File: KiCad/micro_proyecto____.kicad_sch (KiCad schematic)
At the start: 37 parts, among them J1 Conn_01x02, J2 Conn_01x05, J3 Conn_01x02, J4 Conn_01x02, J5 Conn_01x02, J6 Conn_01x02, SW1 SW_Push, SW2 SW_Push, SW3 SW_Push, SW4 SW_Push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

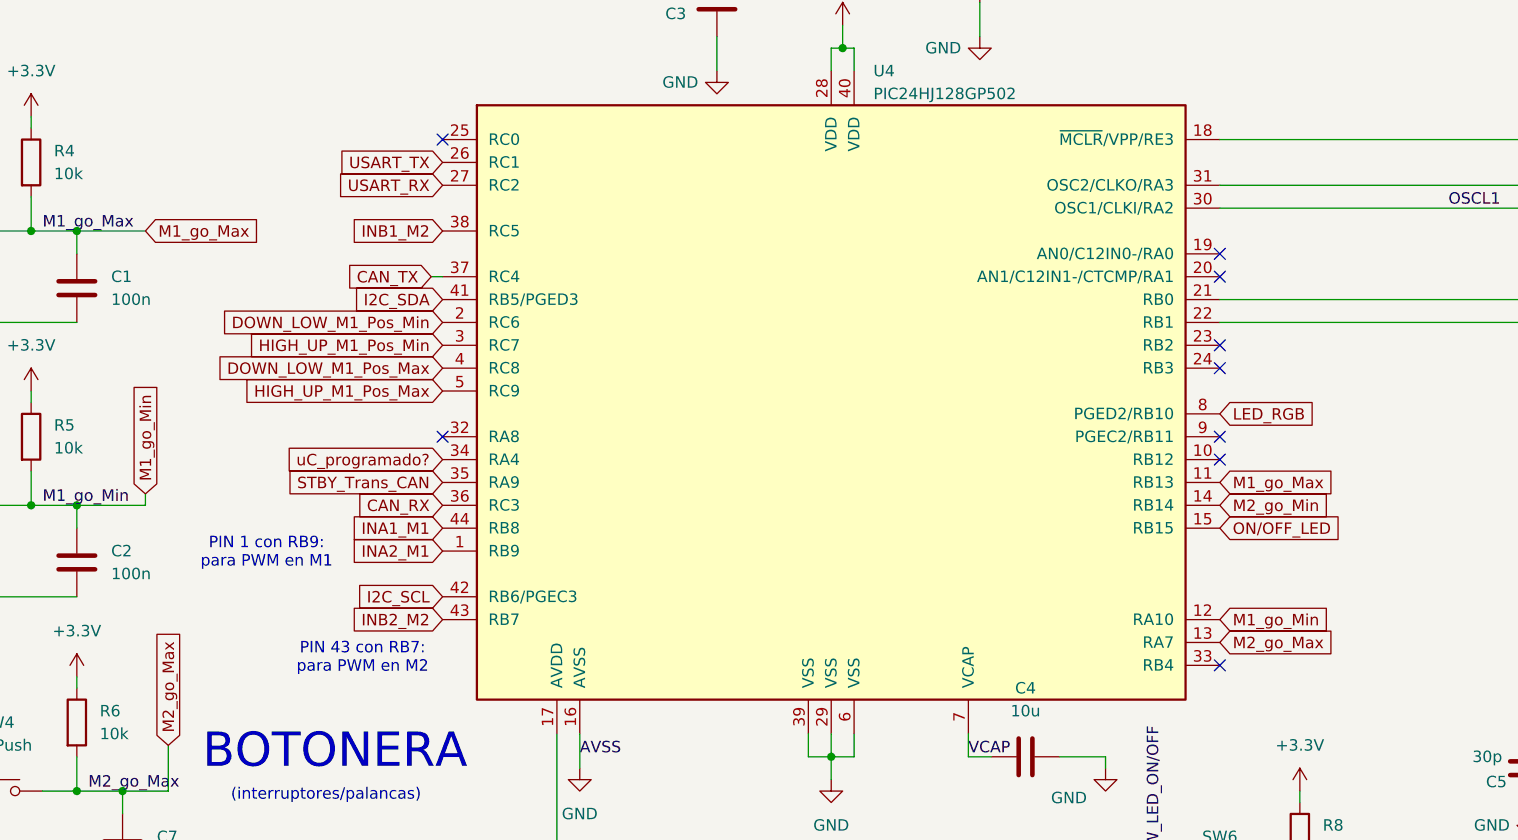
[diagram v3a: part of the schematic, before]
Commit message: PCB casi acabada, despues de revisión de ayer 27/04 y cambio en componente CAN, que se vera reflejado en README y en DB
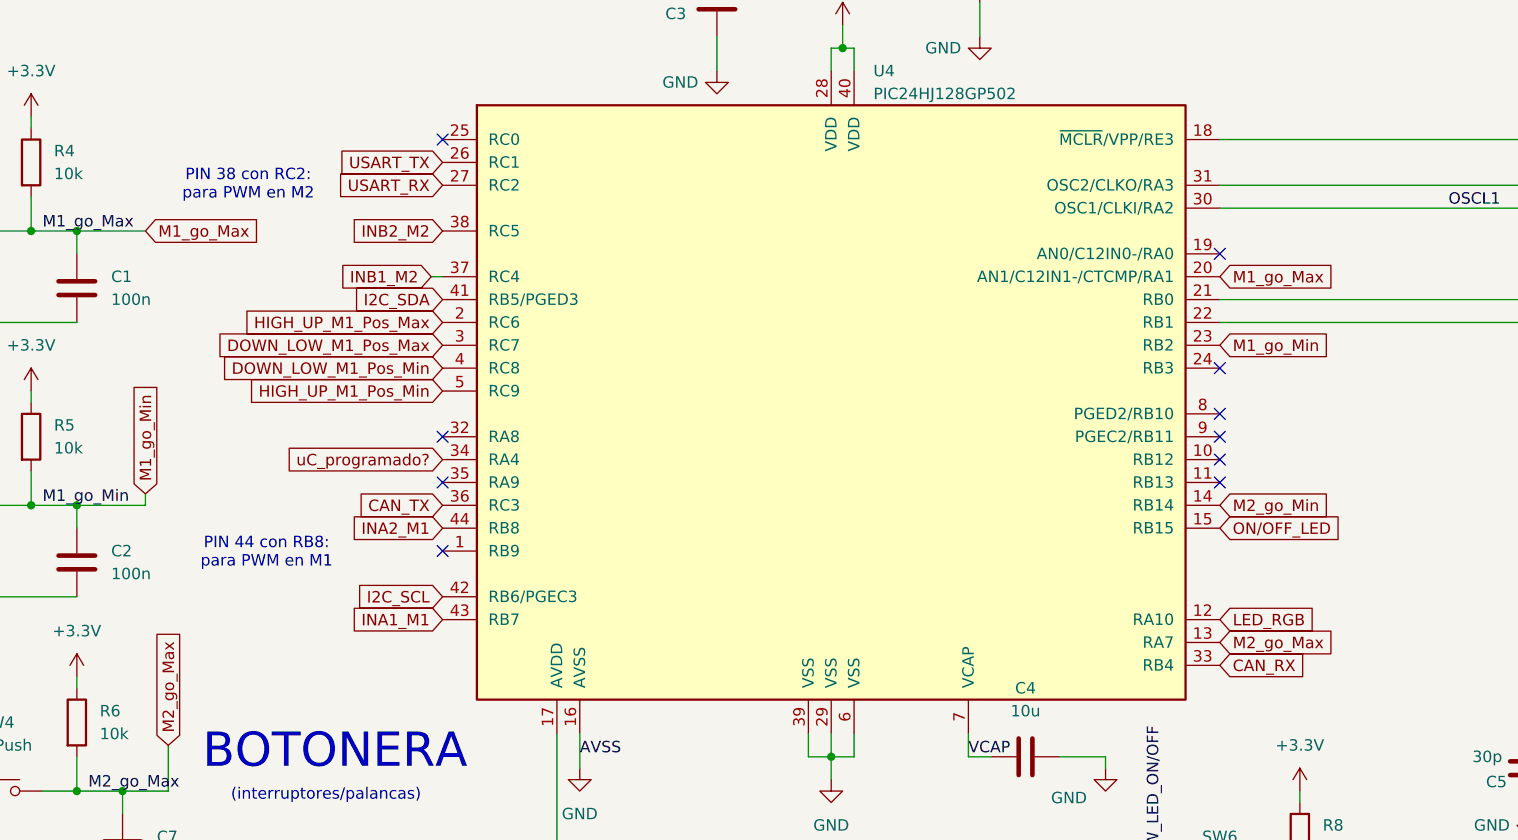
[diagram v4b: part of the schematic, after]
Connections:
- net CAN_RX: now also U4.33 (RB4); no longer U4.36 (RC3)
- net CAN_TX: now also U4.36 (RC3); no longer U4.37 (RC4)
- net DOWN_LOW_M1_Pos_Max: now also U4.3 (RC7); no longer U4.4 (RC8)
- net DOWN_LOW_M1_Pos_Min: now also U4.4 (RC8); no longer U4.2 (RC6)
- net HIGH_UP_M1_Pos_Max: now also U4.2 (RC6); no longer U4.5 (RC9)
- net HIGH_UP_M1_Pos_Min: now also U4.5 (RC9); no longer U4.3 (RC7)
- net INA1_M1: now also U4.43 (RB7); no longer U4.44 (RB8)
- net INA2_M1: now also U4.44 (RB8); no longer U4.1 (RB9)
- net INB1_M2: now also U4.37 (RC4); no longer U4.38 (RC5)
- net INB2_M2: now also U4.38 (RC5); no longer U4.43 (RB7)
- net LED_RGB: now also U4.12 (RA10); no longer U4.8 (PGED2/RB10)
- net M1_go_Max: now also U4.20 (AN1/C12IN1-/CTCMP/RA1); no longer U4.11 (RB13)
- net M1_go_Min: now also U4.23 (RB2); no longer U4.12 (RA10)
- net STBY_Trans_CAN: no longer names the net of U4.35 (RA9)
- no-connect marks 9 -> 10
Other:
- note added: "PIN 38 con RC2: para PWM en M2"
- note added: "PIN 44 con RB8: para PWM en M1"
- note removed: "PIN 1 con RB9: para PWM en M1"
- note removed: "PIN 43 con RB7: para PWM en M2"

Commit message: Layout definitivo
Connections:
- net Conn_SW_M1_Max: no longer J1.2 (Pin_2), SW2.1
- net GND: now also SW2.1, SW3.1, SW4.1, SW5.1, SW6.1
- net M1_go_Max: now also J1.2 (Pin_2)
- net M1_go_Min: now also J3.2 (Pin_2)
- net M2_go_Max: now also J4.2 (Pin_2)
- net M2_go_Min: now also J5.2 (Pin_2)
- net ON/OFF_LED: now also J6.2 (Pin_2)
- removed net Conn_SW_LED_ON/OFF: J6.2 (Pin_2), SW6.1
- removed net Conn_SW_M1_Min: J3.2 (Pin_2), SW3.1
- removed net Conn_SW_M2_Max: J4.2 (Pin_2), SW4.1
- removed net Conn_SW_M2_Min: J5.2 (Pin_2), SW5.1
- net DOWN_LOW_M1_Pos_Max: no longer names the net of U4.3 (RC7)
- net DOWN_LOW_M1_Pos_Min: no longer names the net of U4.4 (RC8)
- net HIGH_UP_M1_Pos_Max renamed Pos_MIN
- net HIGH_UP_M1_Pos_Min renamed Pos_MAX
- no-connect marks 10 -> 12
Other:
- moved on the sheet: J1, J3, J4, J5, J6
